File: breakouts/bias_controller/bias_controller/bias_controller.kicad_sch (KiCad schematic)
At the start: 0 parts

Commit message: bias controller schematic work
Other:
- sheet dac ports: added DAC_DIN, DAC_SCLK, DAC_VDD, DAC_VDD_~{SYNC}, DAC_VPP, DAC_VPP_~{SYNC}, DAC_VSS, DAC_VSS_~{SYNC}, DAC_VT1, DAC_VT1_~{SYNC}, DAC_VT2, DAC_VT2_~{SYNC}; removed none
- sheet load switch ports: added 3V3_SW_EN, VDD_SW_EN; removed none
- sheet mcu ports: added 3V3_SW_EN, DAC_DIN, DAC_SCLK, DAC_VDD_~{SYNC}, DAC_VPP_~{SYNC}, DAC_VSS_~{SYNC}, DAC_VT1_~{SYNC}, DAC_VT2_~{SYNC}, EXT_PIO_1, EXT_PIO_2, EXT_PIO_3, EXT_PIO_4, EXT_PIO_5, EXT_PIO_6, EXT_PIO_7, EXT_PIO_8, EXT_SPI_CSn, EXT_SPI_RX, EXT_SPI_SCK, EXT_SPI_TX, EXT_UART0_RX, EXT_UART0_TX, I2C0_SCL, I2C0_SDA, VDD_SW_EN, VSS_SW_EN; removed none
- sheet power ports: added VSS_SW_EN; removed none

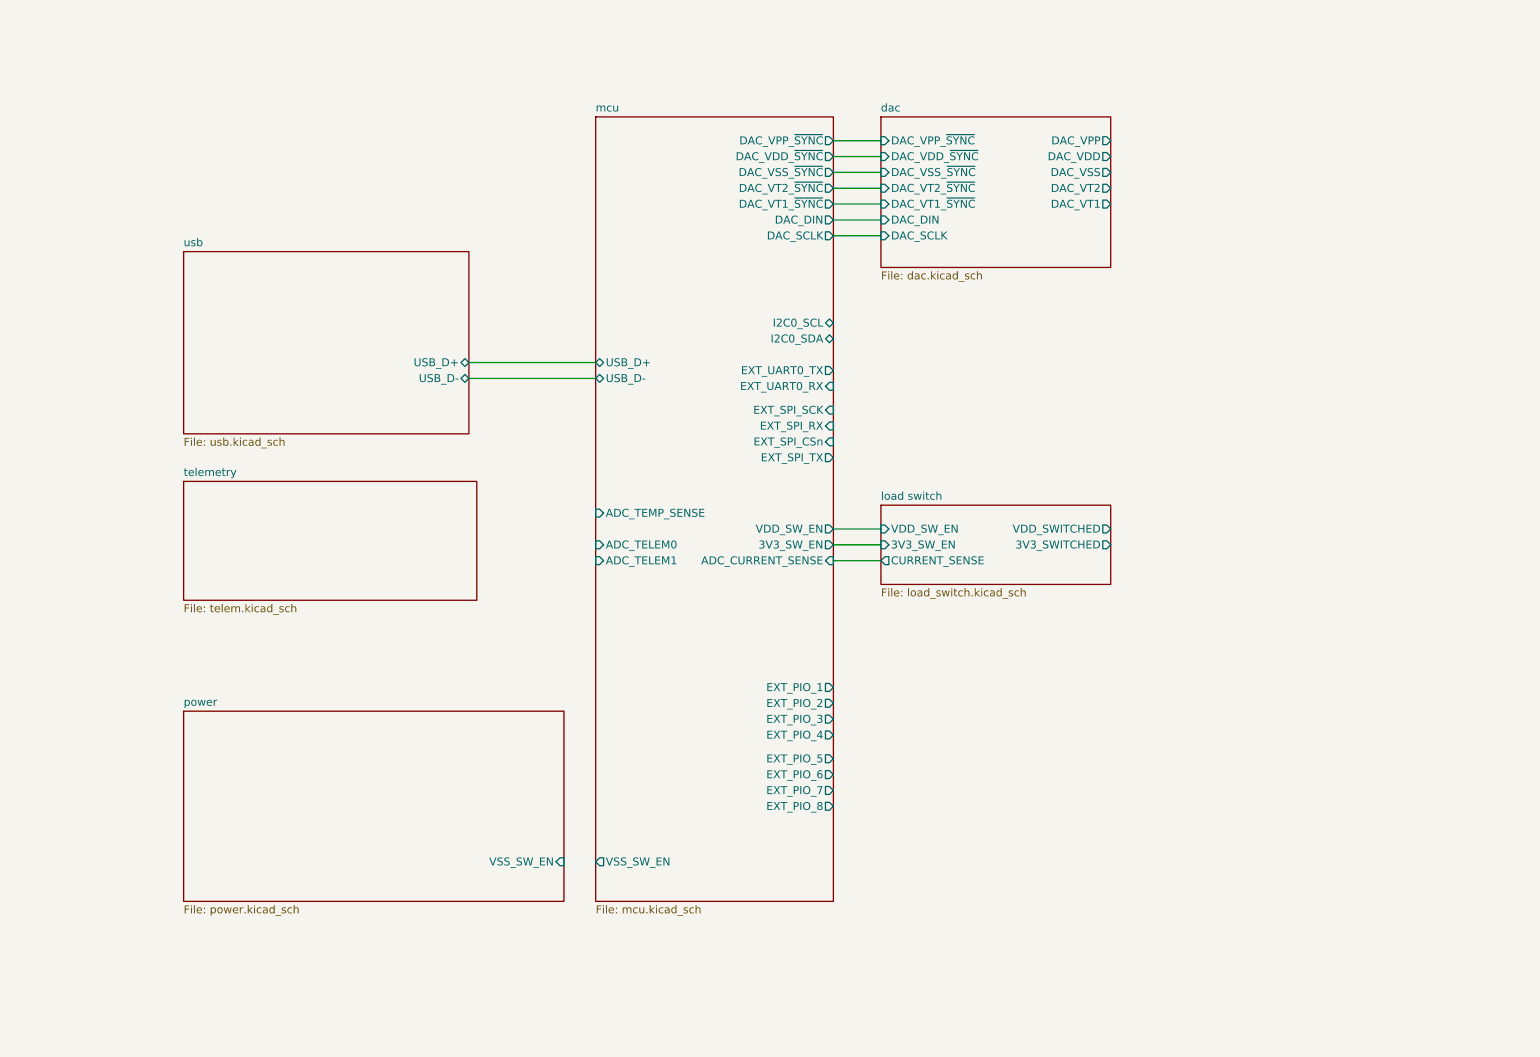
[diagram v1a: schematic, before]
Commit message: top level schematic work
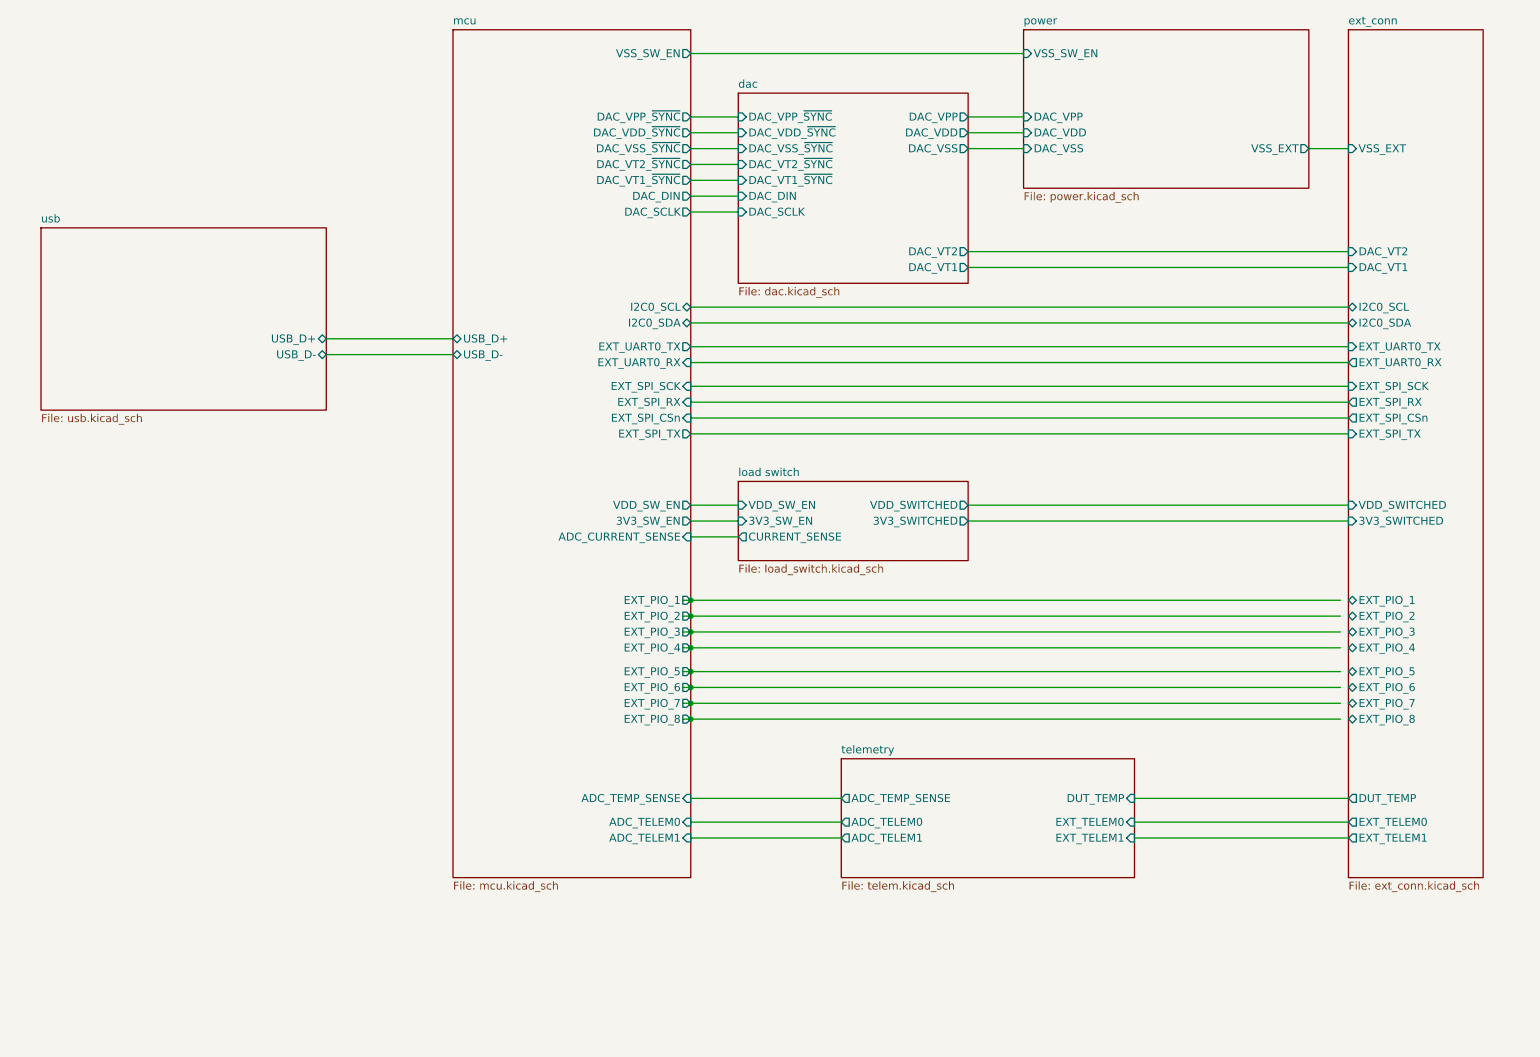
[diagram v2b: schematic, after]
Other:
- added sheet ext_conn (ext_conn.kicad_sch)
- sheet power ports: added DAC_VDD, DAC_VPP, DAC_VSS, VSS_EXT; removed none
- sheet telemetry ports: added ADC_TELEM0, ADC_TELEM1, ADC_TEMP_SENSE, DUT_TEMP, EXT_TELEM0, EXT_TELEM1; removed none

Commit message: more bias controller schematic work
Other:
- sheet ext_conn ports: added none; removed DUT_TEMP
- sheet mcu ports: added none; removed ADC_TEMP_SENSE
- sheet telemetry ports: added none; removed ADC_TEMP_SENSE, DUT_TEMP
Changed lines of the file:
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@@
 (kicad_sch (version 20230819) (generator eeschema)
   (paper "A4")
-  (junction (at 124.46 128.27) (diameter 0) (color 0 0 0 0)
-  )
-  (junction (at 124.46 125.73) (diameter 0) (color 0 0 0 0)
-  )
-  (junction (at 124.46 130.81) (diameter 0) (color 0 0 0 0)
-  )
-  (junction (at 124.46 111.76) (diameter 0) (color 0 0 0 0)
-  )
-  (junction (at 124.46 114.3) (diameter 0) (color 0 0 0 0)
-  )
-  (junction (at 124.46 119.38) (diameter 0) (color 0 0 0 0)
-  )
-  (junction (at 124.46 116.84) (diameter 0) (color 0 0 0 0)
-  )
-  (junction (at 124.46 123.19) (diameter 0) (color 0 0 0 0)
-  )
   (wire (pts (xy 124.46 67.31) (xy 229.87 67.31))
     (stroke (width 0) (type default))
@@
     (stroke (width 0) (type default))
   )
-  (wire (pts (xy 123.19 116.84) (xy 124.46 116.84))
-    (stroke (width 0) (type default))
-  )
   (wire (pts (xy 168.91 55.88) (xy 229.87 55.88))
     (stroke (width 0) (type default))
@@
     (stroke (width 0) (type default))
   )
-  (wire (pts (xy 123.19 123.19) (xy 124.46 123.19))
-    (stroke (width 0) (type default))
-  )
   (wire (pts (xy 124.46 46.99) (xy 132.08 46.99))
     (stroke (width 0) (type default))
@@
     (stroke (width 0) (type default))
   )
-  (wire (pts (xy 123.19 114.3) (xy 124.46 114.3))
-    (stroke (width 0) (type default))
-  )
   (wire (pts (xy 195.58 147.32) (xy 229.87 147.32))
     (stroke (width 0) (type default))
   )
-  (wire (pts (xy 123.19 128.27) (xy 124.46 128.27))
-    (stroke (width 0) (type default))
-  )
   (wire (pts (xy 124.46 39.37) (xy 132.08 39.37))
     (stroke (width 0) (type default))
@@
     (stroke (width 0) (type default))
   )
-  (wire (pts (xy 124.46 111.76) (xy 228.6 111.76))
+  (wire (pts (xy 124.46 111.76) (xy 229.87 111.76))
     (stroke (width 0) (type default))
   )
@@
     (stroke (width 0) (type default))
   )
-  (wire (pts (xy 195.58 143.51) (xy 229.87 143.51))
-    (stroke (width 0) (type default))
-  )
-  (wire (pts (xy 124.46 114.3) (xy 228.6 114.3))
+  (wire (pts (xy 124.46 114.3) (xy 229.87 114.3))
     (stroke (width 0) (type default))
   )
@@
     (stroke (width 0) (type default))
   )
-  (wire (pts (xy 124.46 123.19) (xy 228.6 123.19))
-    (stroke (width 0) (type default))
-  )
-  (wire (pts (xy 124.46 119.38) (xy 228.6 119.38))
-    (stroke (width 0) (type default))
-  )
-  (wire (pts (xy 124.46 143.51) (xy 148.59 143.51))
+  (wire (pts (xy 124.46 123.19) (xy 229.87 123.19))
+    (stroke (width 0) (type default))
+  )
+  (wire (pts (xy 124.46 119.38) (xy 229.87 119.38))
     (stroke (width 0) (type default))
   )
@@
     (stroke (width 0) (type default))
   )
-  (wire (pts (xy 123.19 130.81) (xy 124.46 130.81))
-    (stroke (width 0) (type default))
-  )
   (wire (pts (xy 124.46 101.6) (xy 132.08 101.6))
     (stroke (width 0) (type default))
@@
     (stroke (width 0) (type default))
   )
-  (wire (pts (xy 124.46 125.73) (xy 228.6 125.73))
-    (stroke (width 0) (type default))
-  )
-  (wire (pts (xy 124.46 128.27) (xy 228.6 128.27))
+  (wire (pts (xy 124.46 125.73) (xy 229.87 125.73))
+    (stroke (width 0) (type default))
+  )
+  (wire (pts (xy 124.46 128.27) (xy 229.87 128.27))
     (stroke (width 0) (type default))
   )
@@
     (stroke (width 0) (type default))
   )
-  (wire (pts (xy 124.46 116.84) (xy 228.6 116.84))
-    (stroke (width 0) (type default))
-  )
-  (wire (pts (xy 123.19 111.76) (xy 124.46 111.76))
-    (stroke (width 0) (type default))
-  )
-  (wire (pts (xy 123.19 125.73) (xy 124.46 125.73))
-    (stroke (width 0) (type default))
-  )
-  (wire (pts (xy 124.46 130.81) (xy 228.6 130.81))
+  (wire (pts (xy 124.46 116.84) (xy 229.87 116.84))
+    (stroke (width 0) (type default))
+  )
+  (wire (pts (xy 124.46 130.81) (xy 229.87 130.81))
     (stroke (width 0) (type default))
   )
   (wire (pts (xy 124.46 24.13) (xy 177.8 24.13))
-    (stroke (width 0) (type default))
-  )
-  (wire (pts (xy 123.19 119.38) (xy 124.46 119.38))
     (stroke (width 0) (type default))
   )
@@
       (effects (font (size 1.27 1.27)) (justify left top))
     )
-    (pin "DUT_TEMP" output (at 229.87 143.51 180)
-      (effects (font (size 1.27 1.27)) (justify left))
-    )
     (pin "DAC_VT2" input (at 229.87 55.88 180)
       (effects (font (size 1.27 1.27)) (justify left))
@@
       (effects (font (size 1.27 1.27)) (justify right))
     )
-    (pin "ADC_TEMP_SENSE" input (at 124.46 143.51 0)
-      (effects (font (size 1.27 1.27)) (justify right))
-    )
     (pin "ADC_CURRENT_SENSE" input (at 124.46 101.6 0)
       (effects (font (size 1.27 1.27)) (justify right))
@@
       (effects (font (size 1.27 1.27)) (justify left top))
     )
-    (pin "ADC_TEMP_SENSE" output (at 148.59 143.51 180)
-      (effects (font (size 1.27 1.27)) (justify left))
-    )
     (pin "ADC_TELEM0" output (at 148.59 147.32 180)
       (effects (font (size 1.27 1.27)) (justify left))
@@
       (effects (font (size 1.27 1.27)) (justify right))
     )
-    (pin "DUT_TEMP" input (at 195.58 143.51 0)
-      (effects (font (size 1.27 1.27)) (justify right))
-    )

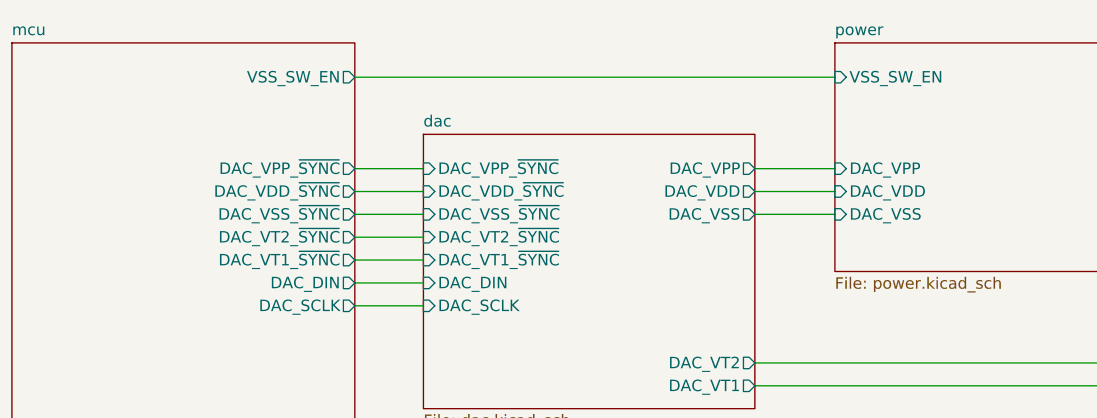
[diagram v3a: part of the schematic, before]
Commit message: bias controller schematic cleanup
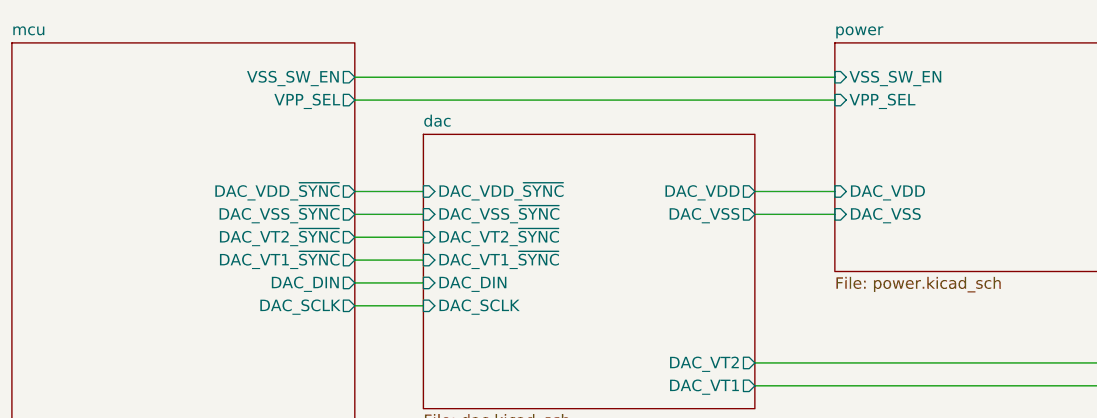
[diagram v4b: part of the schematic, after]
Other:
- sheet dac ports: added none; removed DAC_VPP, DAC_VPP_~{SYNC}
- sheet mcu ports: added VPP_SEL; removed DAC_VPP_~{SYNC}
- sheet power ports: added VPP_SEL; removed DAC_VPP
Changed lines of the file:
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@@
-    (stroke (width 0) (type default))
-  )
-  (wire (pts (xy 124.46 34.29) (xy 132.08 34.29))
     (stroke (width 0) (type default))
   )
@@
     (stroke (width 0) (type default))
   )
+  (wire (pts (xy 124.46 26.67) (xy 177.8 26.67))
+    (stroke (width 0) (type default))
+  )
   (wire (pts (xy 168.91 36.83) (xy 177.8 36.83))
     (stroke (width 0) (type default))
@@
     (stroke (width 0) (type default))
   )
-  (wire (pts (xy 168.91 34.29) (xy 177.8 34.29))
-    (stroke (width 0) (type default))
-  )
   (wire (pts (xy 124.46 125.73) (xy 229.87 125.73))
     (stroke (width 0) (type default))
@@
       (effects (font (size 1.27 1.27)) (justify left))
     )
-    (pin "DAC_VPP" input (at 177.8 34.29 180)
-      (effects (font (size 1.27 1.27)) (justify left))
-    )
     (pin "DAC_VSS" input (at 177.8 39.37 180)
       (effects (font (size 1.27 1.27)) (justify left))
@@
     (pin "VSS_EXT" output (at 223.52 39.37 0)
       (effects (font (size 1.27 1.27)) (justify right))
+    )
+    (pin "VPP_SEL" input (at 177.8 26.67 180)
+      (effects (font (size 1.27 1.27)) (justify left))
     )
     (instances
@@
       (effects (font (size 1.27 1.27)) (justify right))
     )
-    (pin "DAC_VPP_~{SYNC}" output (at 124.46 34.29 0)
-      (effects (font (size 1.27 1.27)) (justify right))
-    )
     (pin "DAC_VSS_~{SYNC}" output (at 124.46 39.37 0)
       (effects (font (size 1.27 1.27)) (justify right))
@@
     )
     (pin "EXT_PIO_8" output (at 124.46 130.81 0)
+      (effects (font (size 1.27 1.27)) (justify right))
+    )
+    (pin "VPP_SEL" output (at 124.46 26.67 0)
       (effects (font (size 1.27 1.27)) (justify right))
     )
@@
       (effects (font (size 1.27 1.27)) (justify left top))
     )
-    (pin "DAC_VPP_~{SYNC}" input (at 132.08 34.29 180)
-      (effects (font (size 1.27 1.27)) (justify left))
-    )
     (pin "DAC_VDD_~{SYNC}" input (at 132.08 36.83 180)
       (effects (font (size 1.27 1.27)) (justify left))
@@
       (effects (font (size 1.27 1.27)) (justify left))
     )
-    (pin "DAC_VPP" output (at 168.91 34.29 0)
-      (effects (font (size 1.27 1.27)) (justify right))
-    )
     (pin "DAC_VSS" output (at 168.91 39.37 0)

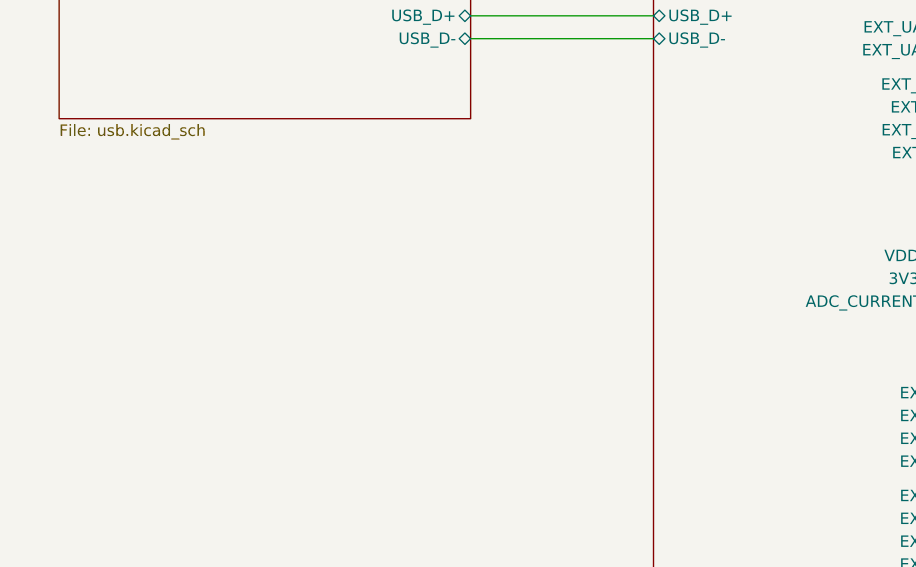
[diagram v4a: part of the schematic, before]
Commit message: most footprint assignments on bias controller board, schematic cleanup
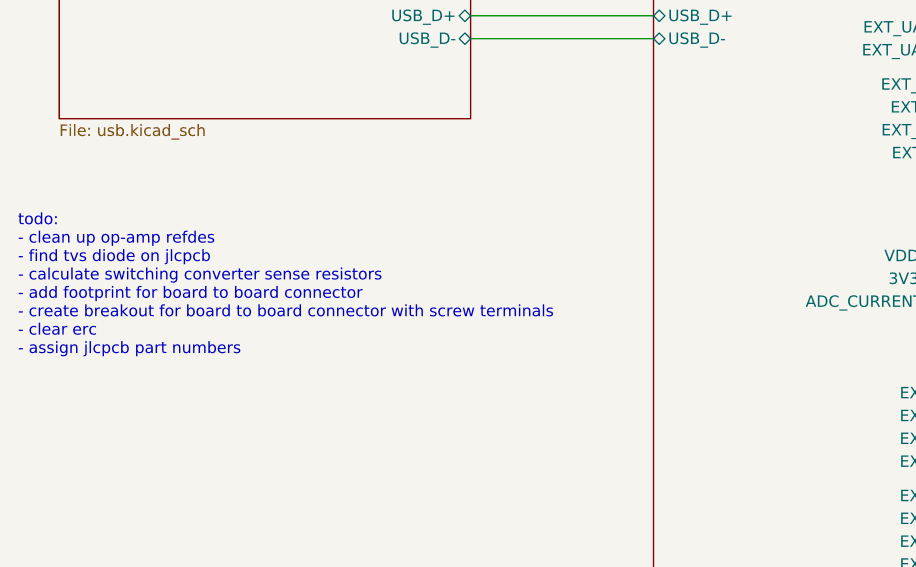
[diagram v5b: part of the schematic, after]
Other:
- note added: "todo: - clean up op-amp refdes - find tvs diode on jlcpcb - calculate switching converter sense resistors - add footprint for board to board connector - create breakout for board to board connector with screw terminals - clear erc - assign jlcpcb part numbers"

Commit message: added board to board connector
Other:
- note added: "todo: - clean up op-amp refdes - add crystal part number - add switch part number - find tvs diode on jlcpcb - calculate switching converter sense resistors - create breakout for board to board connector with screw terminals - clear erc - assign jlcpcb part numbers"
- note removed: "todo: - clean up op-amp refdes - find tvs diode on jlcpcb - calculate switching converter sense resistors - add footprint for board to board connector - create breakout for board to board connector with screw terminals - clear erc - assign jlcpcb part numbers"
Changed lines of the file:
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@@
 		)
 	)
-	(text "todo:\n- clean up op-amp refdes\n- find tvs diode on jlcpcb\n- calculate switching converter sense resistors\n- add footprint for board to board connector\n- create breakout for board to board connector with screw terminals\n- clear erc\n- assign jlcpcb part numbers"
+	(text "todo:\n- clean up op-amp refdes\n- add crystal part number\n- add switch part number\n- find tvs diode on jlcpcb\n- calculate switching converter sense resistors\n- create breakout for board to board connector with screw terminals\n- clear erc\n- assign jlcpcb part numbers"
 		(exclude_from_sim no)
 		(at 15.748 99.822 0)
